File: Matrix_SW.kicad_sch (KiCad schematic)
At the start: 136 parts, among them SW1 ESC, SW10 #9, SW11 #0, SW12 -_, SW13 =+, SW14 BCKSPC, SW15 PGUP, SW16 TAB, SW17 Q, SW18 W, SW19 E, SW2 #1, SW20 R, SW21 T, SW22 Y, SW23 U, SW24 I, SW25 O, SW26 P, SW27 [{, SW28 ]}, SW29 \|, SW3 #2, SW30 PGDN, SW31 CPSLCK, SW32 A, SW33 S, SW34 D, SW35 F, SW36 G, SW37 H, SW38 J, SW39 K, SW4 #3, SW40 L, SW41 ;:, SW42 '", SW43 ENTR, SW44 END, SW45 SHFT, SW46 Z, SW47 X, SW48 C, SW49 V, SW5 #4, SW50 B, SW51 N, SW52 M, SW53 ,<, SW54 .>, SW55 /?, SW56 SHFT, SW57 UP, SW58 DELETE, SW59 CTRL, SW6 #5, SW60 SUPER, SW61 ALT, SW62 SPACE, SW63 ALT, SW64 Fn, SW65 CTRL, SW66 LEFT, SW67 DOWN, SW68 RIGHT, SW7 #6, SW8 #7, SW9 #8

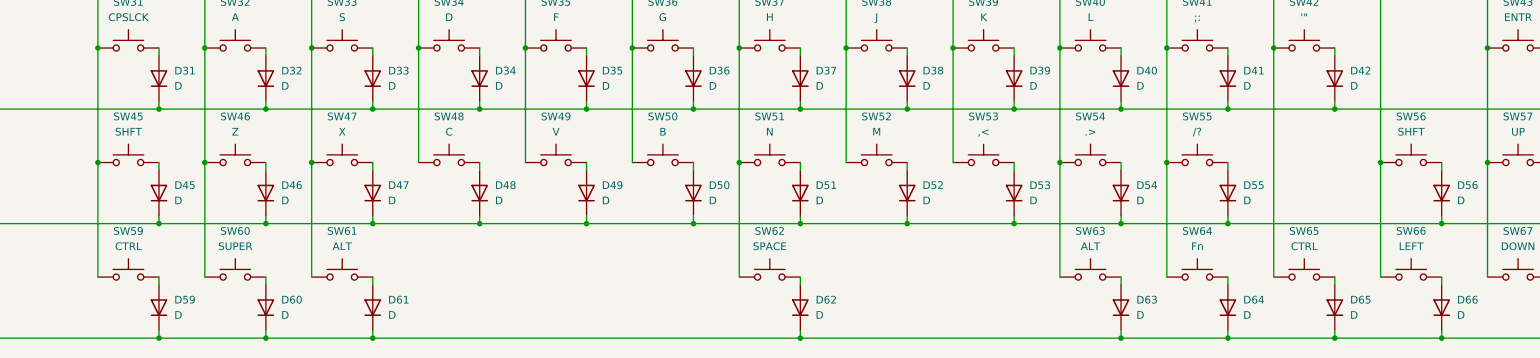
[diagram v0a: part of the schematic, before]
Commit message: Assigning footprint to components
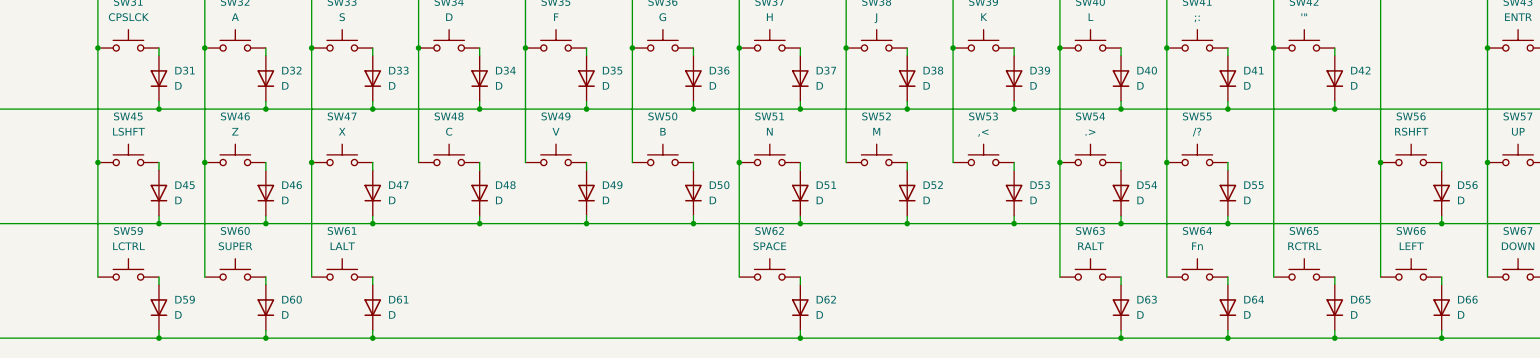
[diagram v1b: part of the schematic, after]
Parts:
- D1, D10, D11, D12, D13, D14, D15, D16, D17, D18, D19, D2, D20, D21, D22, D23, D24, D25, D26, D27, D28, D29, D3, D30, D31, D32, D33, D34, D35, D36, D37, D38, D39, D4, D40, D41, D42, D43, D44, D45, D46, D47, D48, D49, D5, D50, D51, D52, D53, D54, D55, D56, D57, D58, D59, D6, D60, D61, D62, D63, D64, D65, D66, D67, D68, D7, D8, D9: footprint (none) -> Diode_SMD:D_SOD-123
- SW1, SW10, SW11, SW12, SW13, SW15, SW17, SW18, SW19, SW2, SW20, SW21, SW22, SW23, SW24, SW25, SW26, SW27, SW28, SW3, SW30, SW32, SW33, SW34, SW35, SW36, SW37, SW38, SW39, SW4, SW40, SW41, SW42, SW44, SW46, SW47, SW48, SW49, SW5, SW50, SW51, SW52, SW53, SW54, SW55, SW57, SW58, SW6, SW64, SW66, SW67, SW68, SW7, SW8, SW9: footprint (none) -> Switch_Keyboard_Cherry_MX:SW_Cherry_MX_PCB_1.00u
- SW14: footprint (none) -> Switch_Keyboard_Cherry_MX:SW_Cherry_MX_PCB_2.00u
- SW16, SW29, SW60: footprint (none) -> Switch_Keyboard_Cherry_MX:SW_Cherry_MX_PCB_1.50u
- SW31: footprint (none) -> Switch_Keyboard_Cherry_MX:SW_Cherry_MX_PCB_1.75u
- SW43: footprint (none) -> Switch_Keyboard_Cherry_MX:SW_Cherry_MX_PCB_2.25u
- SW45: value SHFT -> LSHFT; footprint (none) -> Switch_Keyboard_Cherry_MX:SW_Cherry_MX_PCB_2.25u
- SW56: value SHFT -> RSHFT; footprint (none) -> Switch_Keyboard_Cherry_MX:SW_Cherry_MX_PCB_1.75u
- SW59: value CTRL -> LCTRL; footprint (none) -> Switch_Keyboard_Cherry_MX:SW_Cherry_MX_PCB_1.50u
- SW61: value ALT -> LALT; footprint (none) -> Switch_Keyboard_Cherry_MX:SW_Cherry_MX_PCB_1.25u
- SW62: footprint (none) -> Switch_Keyboard_Cherry_MX:SW_Cherry_MX_PCB_6.50u
- SW63: value ALT -> RALT; footprint (none) -> Switch_Keyboard_Cherry_MX:SW_Cherry_MX_PCB_1.25u
- SW65: value CTRL -> RCTRL; footprint (none) -> Switch_Keyboard_Cherry_MX:SW_Cherry_MX_PCB_1.00u

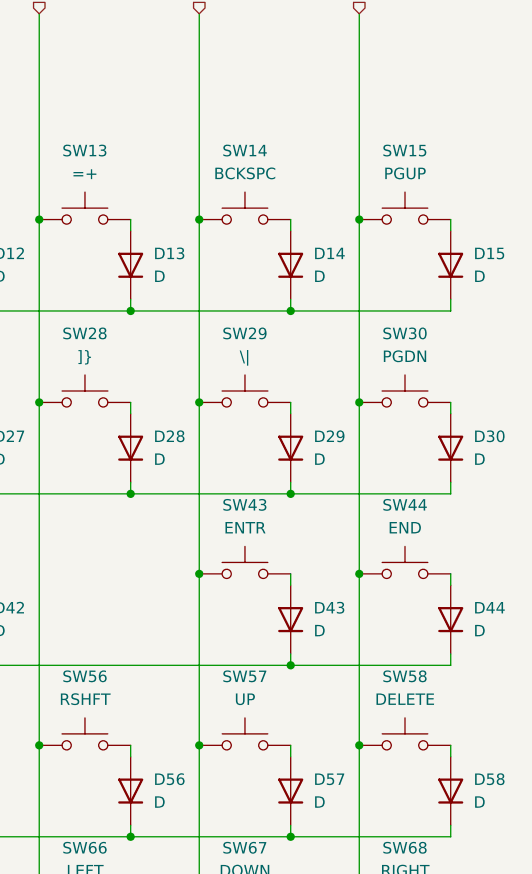
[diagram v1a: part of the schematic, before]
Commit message: Change keyboard layout and reasign keyboard footprints
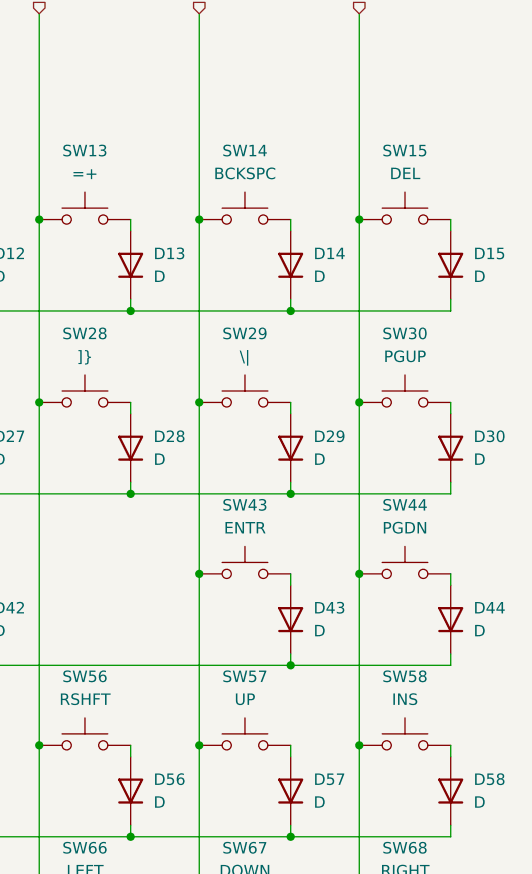
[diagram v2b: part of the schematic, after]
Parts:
- SW15: value PGUP -> DEL
- SW30: value PGDN -> PGUP
- SW44: value END -> PGDN
- SW58: value DELETE -> INS
- SW59: footprint Switch_Keyboard_Cherry_MX:SW_Cherry_MX_PCB_1.50u -> Switch_Keyboard_Cherry_MX:SW_Cherry_MX_PCB_1.25u
- SW60: footprint Switch_Keyboard_Cherry_MX:SW_Cherry_MX_PCB_1.50u -> Switch_Keyboard_Cherry_MX:SW_Cherry_MX_PCB_1.00u
- SW61: footprint Switch_Keyboard_Cherry_MX:SW_Cherry_MX_PCB_1.25u -> Switch_Keyboard_Cherry_MX:SW_Cherry_MX_PCB_1.00u
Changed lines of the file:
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@@
     (property "Reference" "SW60" (id 0) (at 107.95 177.8 0))
     (property "Value" "SUPER" (id 1) (at 107.95 180.34 0))
-    (property "Footprint" "Switch_Keyboard_Cherry_MX:SW_Cherry_MX_PCB_1.50u" (id 2) (at 107.95 180.34 0)
+    (property "Footprint" "Switch_Keyboard_Cherry_MX:SW_Cherry_MX_PCB_1.00u" (id 2) (at 107.95 180.34 0)
       (effects (font (size 1.27 1.27)) hide)
     )
@@
     (property "Reference" "SW59" (id 0) (at 90.17 177.8 0))
     (property "Value" "LCTRL" (id 1) (at 90.17 180.34 0))
-    (property "Footprint" "Switch_Keyboard_Cherry_MX:SW_Cherry_MX_PCB_1.50u" (id 2) (at 90.17 180.34 0)
+    (property "Footprint" "Switch_Keyboard_Cherry_MX:SW_Cherry_MX_PCB_1.25u" (id 2) (at 90.17 180.34 0)
       (effects (font (size 1.27 1.27)) hide)
     )
@@
     (in_bom yes) (on_board yes)
     (property "Reference" "SW58" (id 0) (at 339.09 158.75 0))
-    (property "Value" "DELETE" (id 1) (at 339.09 161.29 0))
+    (property "Value" "INS" (id 1) (at 339.09 161.29 0))
     (property "Footprint" "Switch_Keyboard_Cherry_MX:SW_Cherry_MX_PCB_1.00u" (id 2) (at 339.09 161.29 0)
       (effects (font (size 1.27 1.27)) hide)
@@
     (in_bom yes) (on_board yes)
     (property "Reference" "SW30" (id 0) (at 339.09 120.65 0))
-    (property "Value" "PGDN" (id 1) (at 339.09 123.19 0))
+    (property "Value" "PGUP" (id 1) (at 339.09 123.19 0))
     (property "Footprint" "Switch_Keyboard_Cherry_MX:SW_Cherry_MX_PCB_1.00u" (id 2) (at 339.09 123.19 0)
       (effects (font (size 1.27 1.27)) hide)
@@
     (in_bom yes) (on_board yes)
     (property "Reference" "SW15" (id 0) (at 339.09 100.33 0))
-    (property "Value" "PGUP" (id 1) (at 339.09 102.87 0))
+    (property "Value" "DEL" (id 1) (at 339.09 102.87 0))
     (property "Footprint" "Switch_Keyboard_Cherry_MX:SW_Cherry_MX_PCB_1.00u" (id 2) (at 339.09 102.87 0)
       (effects (font (size 1.27 1.27)) hide)
@@
     (in_bom yes) (on_board yes)
     (property "Reference" "SW44" (id 0) (at 339.09 139.7 0))
-    (property "Value" "END" (id 1) (at 339.09 142.24 0))
+    (property "Value" "PGDN" (id 1) (at 339.09 142.24 0))
     (property "Footprint" "Switch_Keyboard_Cherry_MX:SW_Cherry_MX_PCB_1.00u" (id 2) (at 339.09 142.24 0)
       (effects (font (size 1.27 1.27)) hide)
@@
     (property "Reference" "SW61" (id 0) (at 125.73 177.8 0))
     (property "Value" "LALT" (id 1) (at 125.73 180.34 0))
-    (property "Footprint" "Switch_Keyboard_Cherry_MX:SW_Cherry_MX_PCB_1.25u" (id 2) (at 125.73 180.34 0)
-      (effects (font (size 1.27 1.27)) hide)
-    )
+    (property "Footprint" "Switch_Keyboard_Cherry_MX:SW_Cherry_MX_PCB_1.00u" (id 2) (at 125.73 180.34 0)
+      (effects (font (size 1.27 1.27)) hide)
+    )

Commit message: Reassign footprint SW59 and re-allign keyboard layout
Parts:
- SW59: footprint Switch_Keyboard_Cherry_MX:SW_Cherry_MX_PCB_1.25u -> Switch_Keyboard_Cherry_MX:SW_Cherry_MX_PCB_1.50u
- SW63: footprint Switch_Keyboard_Cherry_MX:SW_Cherry_MX_PCB_1.25u -> Switch_Keyboard_Cherry_MX:SW_Cherry_MX_PCB_1.00u
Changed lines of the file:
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@@
     (property "Reference" "SW63" (id 0) (at 250.19 177.8 0))
     (property "Value" "RALT" (id 1) (at 250.19 180.34 0))
-    (property "Footprint" "Switch_Keyboard_Cherry_MX:SW_Cherry_MX_PCB_1.25u" (id 2) (at 250.19 180.34 0)
+    (property "Footprint" "Switch_Keyboard_Cherry_MX:SW_Cherry_MX_PCB_1.00u" (id 2) (at 250.19 180.34 0)
       (effects (font (size 1.27 1.27)) hide)
     )
@@
     (property "Reference" "SW59" (id 0) (at 90.17 177.8 0))
     (property "Value" "LCTRL" (id 1) (at 90.17 180.34 0))
-    (property "Footprint" "Switch_Keyboard_Cherry_MX:SW_Cherry_MX_PCB_1.25u" (id 2) (at 90.17 180.34 0)
-      (effects (font (size 1.27 1.27)) hide)
-    )
+    (property "Footprint" "Switch_Keyboard_Cherry_MX:SW_Cherry_MX_PCB_1.50u" (id 2) (at 90.17 180.34 0)
+      (effects (font (size 1.27 1.27)) hide)
+    )

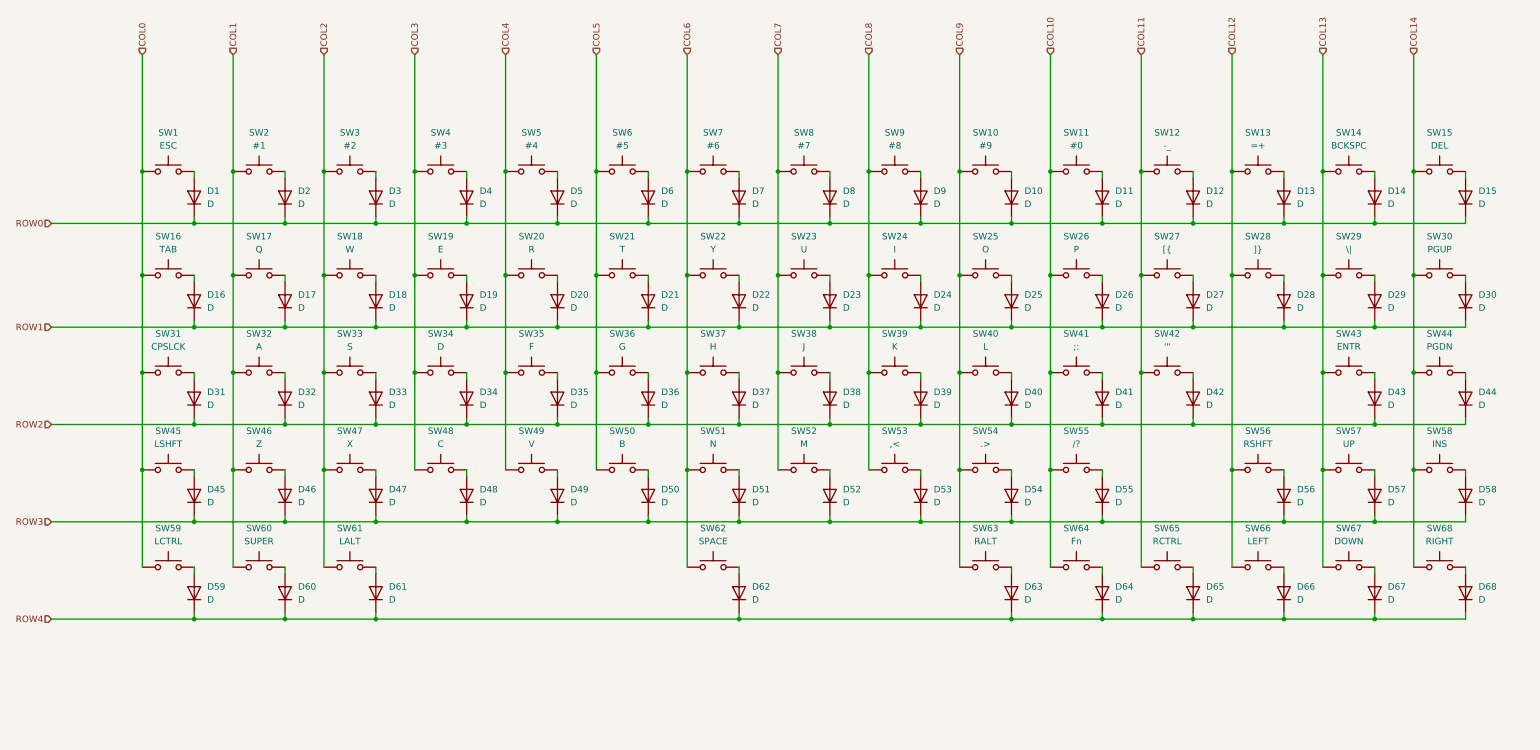
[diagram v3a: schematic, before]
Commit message: Change Diode to more specific type 1N4148 SOD-123
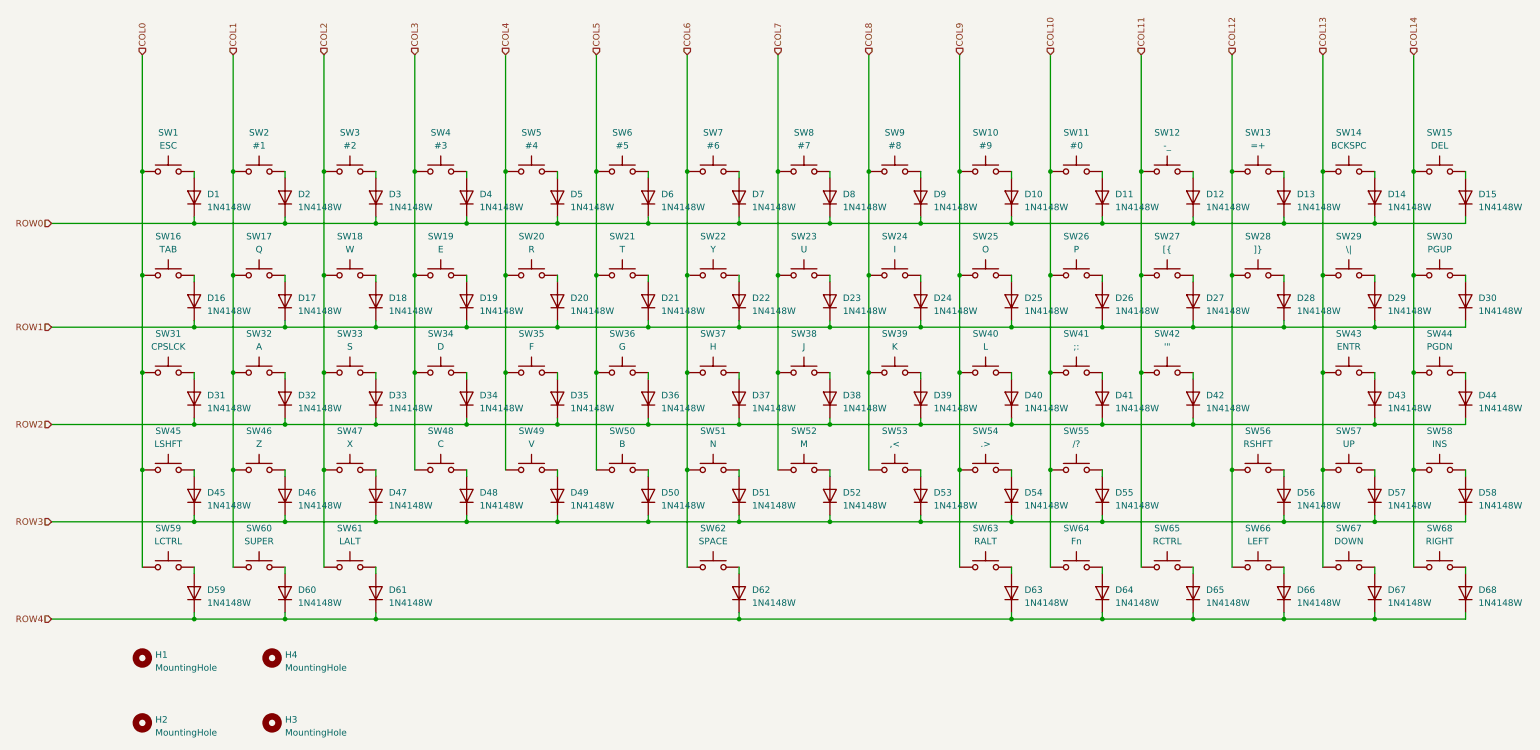
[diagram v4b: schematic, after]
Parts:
- removed D1, D10, D11, D12, D13, D14, D15, D16, D17, D18, D19, D2, D20, D21, D22, D23, D24, D25, D26, D27, D28, D29, D3, D30, D31, D32, D33, D34, D35, D36, D37, D38, D39, D4, D40, D41, D42, D43, D44, D45, D46, D47, D48, D49, D5, D50, D51, D52, D53, D54, D55, D56, D57, D58, D59, D6, D60, D61, D62, D63, D64, D65, D66, D67, D68, D7, D8, D9: D, Diode_SMD:D_SOD-123, symbol Device:D
- added D1, D10, D11, D12, D13, D14, D15, D16, D17, D18, D19, D2, D20, D21, D22, D23, D24, D25, D26, D27, D28, D29, D3, D30, D31, D32, D33, D34, D35, D36, D37, D38, D39, D4, D40, D41, D42, D43, D44, D45, D46, D47, D48, D49, D5, D50, D51, D52, D53, D54, D55, D56, D57, D58, D59, D6, D60, D61, D62, D63, D64, D65, D66, D67, D68, D7, D8, D9: 1N4148W, Diode_SMD:D_SOD-123, symbol Diode:1N4148W
- added H1: MountingHole, Local_lib_Mounting_Keyboard_Stabilizer:Stabilizer_Cherry_MX_6.25u, symbol Mechanical:MountingHole
- added H2, H3, H4: MountingHole, Local_lib_Mounting_Keyboard_Stabilizer:Stabilizer_Cherry_MX_2.00u, symbol Mechanical:MountingHole
- SW1, SW10, SW11, SW12, SW13, SW15, SW17, SW18, SW19, SW2, SW20, SW21, SW22, SW23, SW24, SW25, SW26, SW27, SW28, SW3, SW30, SW32, SW33, SW34, SW35, SW36, SW37, SW38, SW39, SW4, SW40, SW41, SW42, SW44, SW46, SW47, SW48, SW49, SW5, SW50, SW51, SW52, SW53, SW54, SW55, SW57, SW58, SW6, SW60, SW61, SW63, SW64, SW65, SW66, SW67, SW68, SW7, SW8, SW9: footprint Switch_Keyboard_Cherry_MX:SW_Cherry_MX_PCB_1.00u -> Local_lib_Switch_Keyboard_Cherry_MX:SW_Cherry_MX_PCB_1.00u
- SW14: footprint Switch_Keyboard_Cherry_MX:SW_Cherry_MX_PCB_2.00u -> Local_lib_Switch_Keyboard_Cherry_MX:SW_Cherry_MX_PCB_2.00u
- SW16, SW29, SW59: footprint Switch_Keyboard_Cherry_MX:SW_Cherry_MX_PCB_1.50u -> Local_lib_Switch_Keyboard_Cherry_MX:SW_Cherry_MX_PCB_1.50u
- SW31, SW56: footprint Switch_Keyboard_Cherry_MX:SW_Cherry_MX_PCB_1.75u -> Local_lib_Switch_Keyboard_Cherry_MX:SW_Cherry_MX_PCB_1.75u
- SW43, SW45: footprint Switch_Keyboard_Cherry_MX:SW_Cherry_MX_PCB_2.25u -> Local_lib_Switch_Keyboard_Cherry_MX:SW_Cherry_MX_PCB_2.25u
- SW62: footprint Switch_Keyboard_Cherry_MX:SW_Cherry_MX_PCB_6.50u -> Local_lib_Switch_Keyboard_Cherry_MX:SW_Cherry_MX_PCB_6.50u
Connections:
- net ROW0: now also D1.1 (K), D10.1 (K), D11.1 (K), D12.1 (K), D13.1 (K), D14.1 (K), D15.1 (K), D2.1 (K), D3.1 (K), D4.1 (K), D5.1 (K), D6.1 (K), D7.1 (K), D8.1 (K), D9.1 (K)
- net ROW1: now also D16.1 (K), D17.1 (K), D18.1 (K), D19.1 (K), D20.1 (K), D21.1 (K), D22.1 (K), D23.1 (K), D24.1 (K), D25.1 (K), D26.1 (K), D27.1 (K), D28.1 (K), D29.1 (K), D30.1 (K)
- net ROW2: now also D31.1 (K), D32.1 (K), D33.1 (K), D34.1 (K), D35.1 (K), D36.1 (K), D37.1 (K), D38.1 (K), D39.1 (K), D40.1 (K), D41.1 (K), D42.1 (K), D43.1 (K), D44.1 (K)
- net ROW3: now also D45.1 (K), D46.1 (K), D47.1 (K), D48.1 (K), D49.1 (K), D50.1 (K), D51.1 (K), D52.1 (K), D53.1 (K), D54.1 (K), D55.1 (K), D56.1 (K), D57.1 (K), D58.1 (K)
- net ROW4: now also D59.1 (K), D60.1 (K), D61.1 (K), D62.1 (K), D63.1 (K), D64.1 (K), D65.1 (K), D66.1 (K), D67.1 (K), D68.1 (K)
- net at SW36.2: now also D36.2 (A)
- net at SW55.2: now also D55.2 (A)
- net at SW53.2: now also D53.2 (A)
- net at SW32.2: now also D32.2 (A)
- net at SW14.2: now also D14.2 (A)
- net at SW62.2: now also D62.2 (A)
- net at SW13.2: now also D13.2 (A)
- net at SW24.2: now also D24.2 (A)
- net at SW21.2: now also D21.2 (A)
- net at SW68.2: now also D68.2 (A)
- net at SW63.2: now also D63.2 (A)
- net at SW30.2: now also D30.2 (A)
- net at SW18.2: now also D18.2 (A)
- net at SW35.2: now also D35.2 (A)
- net at SW45.2: now also D45.2 (A)
- net at SW60.2: now also D60.2 (A)
- net at SW3.2: now also D3.2 (A)
- net at SW52.2: now also D52.2 (A)
- net at SW19.2: now also D19.2 (A)
- net at SW17.2: now also D17.2 (A)
- net at SW33.2: now also D33.2 (A)
- net at SW12.2: now also D12.2 (A)
- net at SW67.2: now also D67.2 (A)
- net at SW4.2: now also D4.2 (A)
- net at SW59.2: now also D59.2 (A)
- net at SW51.2: now also D51.2 (A)
- net at SW38.2: now also D38.2 (A)
- net at SW34.2: now also D34.2 (A)
- net at SW66.2: now also D66.2 (A)
- net at SW58.2: now also D58.2 (A)
- net at SW43.2: now also D43.2 (A)
- net at SW2.2: now also D2.2 (A)
- net at SW15.2: now also D15.2 (A)
- net at SW47.2: now also D47.2 (A)
- net at SW56.2: now also D56.2 (A)
- net at SW10.2: now also D10.2 (A)
- net at SW64.2: now also D64.2 (A)
- net at SW39.2: now also D39.2 (A)
- net at SW11.2: now also D11.2 (A)
- net at SW42.2: now also D42.2 (A)
- net at SW50.2: now also D50.2 (A)
- net at SW26.2: now also D26.2 (A)
- net at SW29.2: now also D29.2 (A)
- net at SW16.2: now also D16.2 (A)
- net at SW61.2: now also D61.2 (A)
- net at SW7.2: now also D7.2 (A)
- net at SW23.2: now also D23.2 (A)
- net at SW48.2: now also D48.2 (A)
- net at SW40.2: now also D40.2 (A)
- net at SW20.2: now also D20.2 (A)
- net at SW57.2: now also D57.2 (A)
- net at SW37.2: now also D37.2 (A)
- net at SW46.2: now also D46.2 (A)
- net at SW31.2: now also D31.2 (A)
- net at SW41.2: now also D41.2 (A)
- net at SW25.2: now also D25.2 (A)
- net at SW27.2: now also D27.2 (A)
- net at SW6.2: now also D6.2 (A)
- net at SW54.2: now also D54.2 (A)
- net at SW28.2: now also D28.2 (A)
- net at SW1.2: now also D1.2 (A)
- net at SW65.2: now also D65.2 (A)
- net at SW44.2: now also D44.2 (A)
- net at SW49.2: now also D49.2 (A)
- net at SW8.2: now also D8.2 (A)
- net at SW22.2: now also D22.2 (A)
- net at SW9.2: now also D9.2 (A)
- net at SW5.2: now also D5.2 (A)

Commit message: Re-assign symbol and footprint to match local library
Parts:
- H1: footprint Local_lib_Mounting_Keyboard_Stabilizer:Stabilizer_Cherry_MX_6.25u -> Local_Lib:Stabilizer_Cherry_MX_6.25u
- H2, H3, H4: footprint Local_lib_Mounting_Keyboard_Stabilizer:Stabilizer_Cherry_MX_2.00u -> Local_Lib:Stabilizer_Cherry_MX_2.00u
- SW1, SW10, SW11, SW12, SW13, SW15, SW17, SW18, SW19, SW2, SW20, SW21, SW22, SW23, SW24, SW25, SW26, SW27, SW28, SW3, SW30, SW32, SW33, SW34, SW35, SW36, SW37, SW38, SW39, SW4, SW40, SW41, SW42, SW44, SW46, SW47, SW48, SW49, SW5, SW50, SW51, SW52, SW53, SW54, SW55, SW57, SW58, SW6, SW60, SW61, SW63, SW64, SW65, SW66, SW67, SW68, SW7, SW8, SW9: footprint Local_lib_Switch_Keyboard_Cherry_MX:SW_Cherry_MX_PCB_1.00u -> Local_Lib:SW_Cherry_MX_PCB_1.00u
- SW14: footprint Local_lib_Switch_Keyboard_Cherry_MX:SW_Cherry_MX_PCB_2.00u -> Local_Lib:SW_Cherry_MX_PCB_2.00u
- SW16, SW29, SW59: footprint Local_lib_Switch_Keyboard_Cherry_MX:SW_Cherry_MX_PCB_1.50u -> Local_Lib:SW_Cherry_MX_PCB_1.50u
- SW31, SW56: footprint Local_lib_Switch_Keyboard_Cherry_MX:SW_Cherry_MX_PCB_1.75u -> Local_Lib:SW_Cherry_MX_PCB_1.75u
- SW43, SW45: footprint Local_lib_Switch_Keyboard_Cherry_MX:SW_Cherry_MX_PCB_2.25u -> Local_Lib:SW_Cherry_MX_PCB_2.25u
- SW62: footprint Local_lib_Switch_Keyboard_Cherry_MX:SW_Cherry_MX_PCB_6.50u -> Local_Lib:SW_Cherry_MX_PCB_6.50u
